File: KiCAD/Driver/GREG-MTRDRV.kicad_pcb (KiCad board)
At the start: 2 copper layers, 85 parts, among them J1 MOTOR1, J2 MOTOR2, J3 MOTOR1, J4 MOTOR2, J5 MOTOR1, J6 MOTOR2, J7 XT60-M, SW1 SW_Push, U1 STM32G474RETx, U2 DRV8262DDWR, U3 DRV8262DDWR, U4 DRV8262DDWR, U5 TPS543B20RVFT, U6 LMR51430, Y1 24MHz

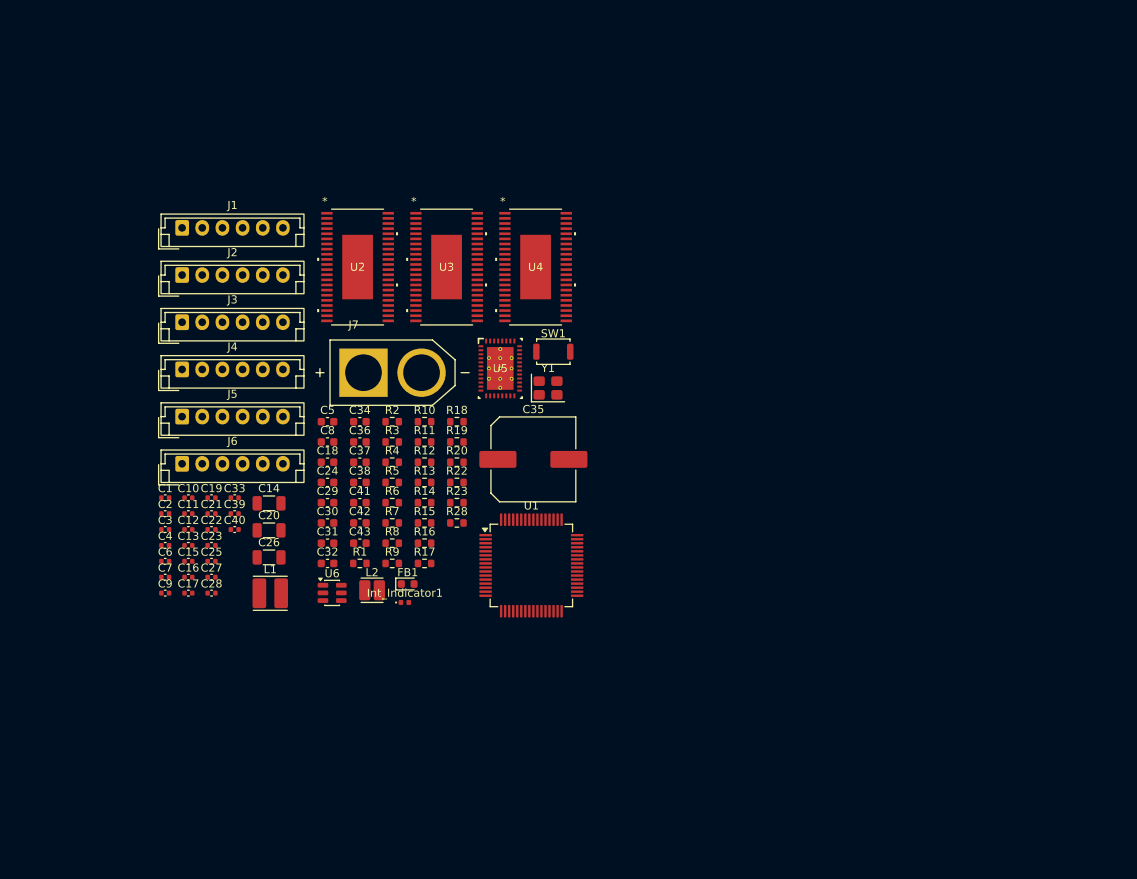
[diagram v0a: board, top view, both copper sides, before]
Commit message: Add journal and update readme
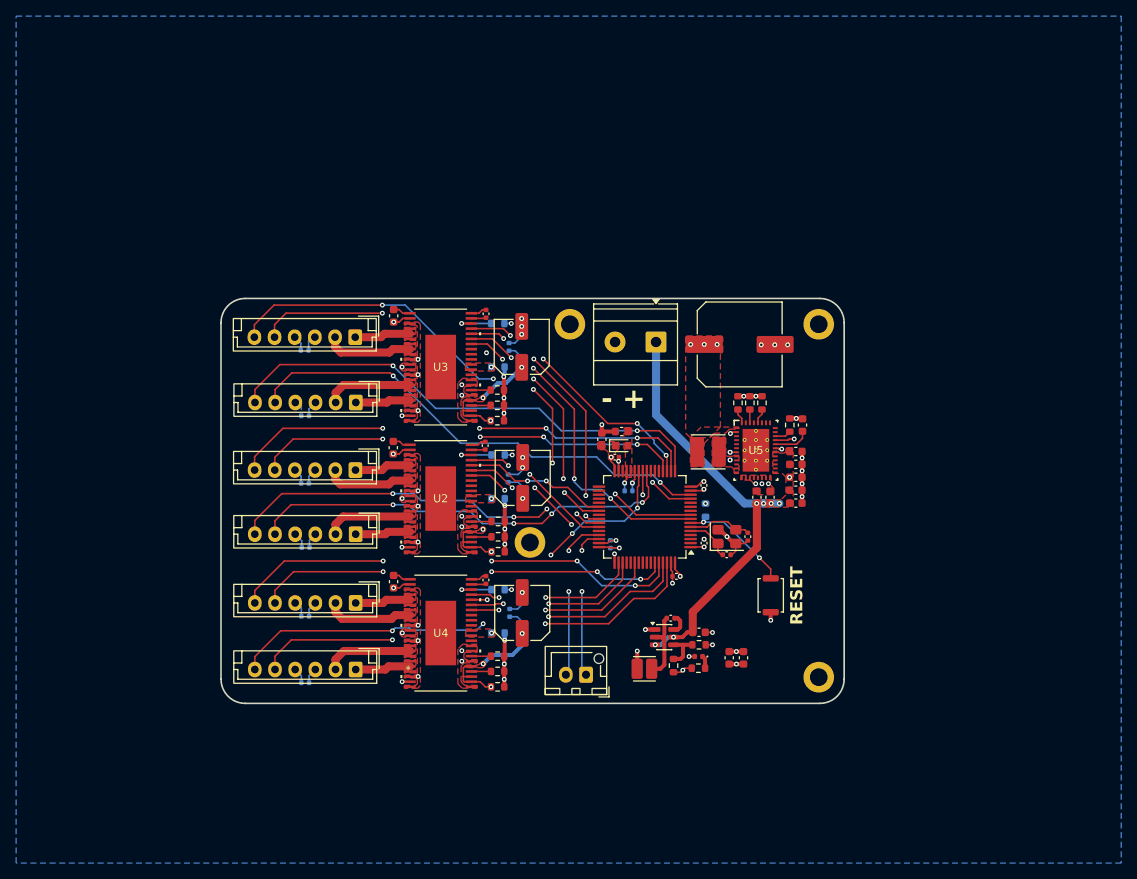
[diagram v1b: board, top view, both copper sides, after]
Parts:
- added J8: Conn_01x02_Pin, 2PinJST:JST_XH_B2B-XH-AM_1x02_P2.50mm_Vertical, F.Cu at (170.7, 131.7)
- added REF**: MountingHole_2.2mm_M2_DIN965_Pad, MountingHole:MountingHole_2.2mm_M2_DIN965_Pad, F.Cu at (163.7, 115.2)
- added REF**: MountingHole_2.2mm_M2_DIN965_Pad, MountingHole:MountingHole_2.2mm_M2_DIN965_Pad, F.Cu at (199.5, 88.2)
- added REF**: MountingHole_2.2mm_M2_DIN965_Pad, MountingHole:MountingHole_2.2mm_M2_DIN965_Pad, F.Cu at (199.5, 131.9)
- added REF**: MountingHole_2.2mm_M2_DIN965_Pad, MountingHole:MountingHole_2.2mm_M2_DIN965_Pad, F.Cu at (168.7, 88.2)
- C12: footprint Capacitor_SMD:C_0402_1005Metric -> Capacitor_SMD:C_0603_1608Metric
- C13, C15, C16, C19, C21, C22, C25, C27, C28, C3, C33, C39, C7, R1, R12, R13, R2, R4, R7, R8: moved to B.Cu
- C14, C20, C26: footprint Capacitor_SMD:C_1206_3216Metric -> Capacitor_SMD:C_Elec_6.3x7.7
- J7: value XT60-M -> PWR; footprint footprint:AMASS_XT60-M -> TerminalBlock_Phoenix:TerminalBlock_Phoenix_MKDS-1,5-2-5.08_1x02_P5.08mm_Horizontal
- moved C9 72.6 mm to (190.7, 114.5), turned to -90 degrees
- moved C10 67.1 mm to (188.1, 116.8)
- moved C2 66.9 mm to (185.3, 108.2), turned to -90 degrees
- moved C6 66.8 mm to (185.3, 115.3), turned to 90 degrees
- moved C4 63.5 mm to (181.8, 119.5), turned to 180 degrees
- moved C33 61.6 mm to (188.5, 104.5), turned to -90 degrees
- moved C32 59.7 mm to (196.7, 104.0)
- moved C31 58.4 mm to (196.7, 108.8)
- moved C7 58.4 mm to (175.9, 108.8)
- moved C29 58.1 mm to (196.7, 107.2)
- moved C30 58.1 mm to (196.7, 110.4)
- moved L1 57.0 mm to (185.8, 104.0), turned to 180 degrees
- moved C1 56.0 mm to (174.2, 104.7)
- moved C3 55.2 mm to (173.7, 115.5), turned to 90 degrees
- moved C40 55.2 mm to (181.2, 124.6), turned to 180 degrees
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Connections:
- C11 pad 1: /CPL1 -> /C1PL1
- C11 pad 2: /CPH1 -> /C1PH1
- C12 pad 2: +3.3V -> VCC
- C13 pad 1: +3.3V -> VCC
- C14 pad 1: +3.3V -> VCC
- C17 pad 1: /CPL1 -> /C2PL1
- C17 pad 2: /CPH1 -> /C2PH1
- C18 pad 1: /VCP1 -> /VCP2
- C18 pad 2: +3.3V -> VCC
- C19 pad 1: +3.3V -> VCC
- C20 pad 1: +3.3V -> VCC
- C23 pad 1: /CPL1 -> /C3PL1
- C23 pad 2: /CPH1 -> /C3PH1
- C24 pad 1: /VCP1 -> /VCP3
- C24 pad 2: +3.3V -> VCC
- C25 pad 1: +3.3V -> VCC
- C26 pad 1: +3.3V -> VCC
- C29 pad 1: +3.3V -> VCC
- C30 pad 1: +3.3V -> VCC
- C31 pad 1: +3.3V -> VCC
- C32 pad 1: +3.3V -> VCC
- C34 pad 1: GNDA -> GND
- C34 pad 2: +3.3V -> VCC
- C35 pad 2: GNDA -> GND
- C37 pad 1: +3.3V -> VCC
- C38 pad 1: +3.3V -> VCC
- C43 pad 1: +3.3V -> VCC
- R11 pad 2: /DVDD -> VCC
- R16 pad 2: /DVDD -> VCC
- R17 pad 2: GNDA -> GND
- R18 pad 1: GNDA -> GND
- R19 pad 1: GNDA -> GND
- R20 pad 1: GNDA -> GND
- R6 pad 2: /DVDD -> VCC
- U2 pad 1: /VCP1 -> /VCP2
- U2 pad 11: +3.3V -> VCC
- U2 pad 12: +3.3V -> VCC
- U2 pad 2: +3.3V -> VCC
- U2 pad 21: +3.3V -> VCC
- U2 pad 24: /DVDD -> VCC
- U2 pad 25: +3.3V -> VCC
- U2 pad 27: /DVDD -> VCC
- U2 pad 43: /CPL1 -> /C2PL1
- U2 pad 44: /CPH1 -> /C2PH1
- U3 pad 11: +3.3V -> VCC
- U3 pad 12: +3.3V -> VCC
- U3 pad 2: +3.3V -> VCC
- U3 pad 21: +3.3V -> VCC
- U3 pad 24: /DVDD -> VCC
- U3 pad 25: +3.3V -> VCC
- U3 pad 27: /DVDD -> VCC
- U3 pad 43: /CPL1 -> /C1PL1
- U3 pad 44: /CPH1 -> /C1PH1
- U4 pad 1: /VCP1 -> /VCP3
- U4 pad 11: +3.3V -> VCC
- U4 pad 12: +3.3V -> VCC
- U4 pad 2: +3.3V -> VCC
- U4 pad 21: +3.3V -> VCC
- U4 pad 24: /DVDD -> VCC
- U4 pad 25: +3.3V -> VCC
- U4 pad 27: /DVDD -> VCC
- U4 pad 43: /CPL1 -> /C3PL1
- U4 pad 44: /CPH1 -> /C3PH1
- U5 pad 21: +3.3V -> VCC
- U5 pad 22: +3.3V -> VCC
- U5 pad 23: +3.3V -> VCC
- U5 pad 24: +3.3V -> VCC
- U5 pad 25: +3.3V -> VCC
- U5 pad 26: +3.3V -> VCC
- U5 pad 29: GNDA -> GND
- U6 pad 3: +3.3V -> VCC
- U6 pad 5: +3.3V -> VCC
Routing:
- net VCC: track 0.00 -> 218.4 mm, vias 0 -> 25
- net /ENC1B: track 0.00 -> 66.5 mm, vias 0 -> 3
- net GND: track 0.00 -> 63.5 mm, vias 0 -> 50
- net /ENC2B: track 0.00 -> 62.4 mm, vias 0 -> 2
- net /ENC2A: track 0.00 -> 60.2 mm, vias 0 -> 2
- net /ENC1A: track 0.00 -> 60.2 mm, vias 0 -> 5
- net /ENC6B: track 0.00 -> 59.5 mm, vias 0 -> 3
- net /ENC3B: track 0.00 -> 58.4 mm, vias 0 -> 4
- net /ENC5B: track 0.00 -> 56.6 mm, vias 0 -> 4
- net /ENC4B: track 0.00 -> 56.5 mm, vias 0 -> 4
- net /ENC6A: track 0.00 -> 55.9 mm, vias 0 -> 2
- net /ENC4A: track 0.00 -> 54.4 mm, vias 0 -> 4
- net /ENC3A: track 0.00 -> 53.3 mm, vias 0 -> 4
- net /ENC5A: track 0.00 -> 51.5 mm, vias 0 -> 4
- net /M1_IN2: track 0.00 -> 42.0 mm, vias 0 -> 4
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- added copper zone on F.Cu, net +3.3V
- added copper zone on In1.Cu, net +3.3V
- added copper zone on B.Cu, net +5V
- added copper zone on F.Cu, net /M1OUT1
- added copper zone on F.Cu, net /M1OUT2
- added copper zone on F.Cu, net /M2OUT1
- added copper zone on F.Cu, net /M2OUT2
- added copper zone on F.Cu, net /M3OUT1
- added copper zone on F.Cu, net /M3OUT2
- added copper zone on F.Cu, net /M4OUT1
- added copper zone on F.Cu, net /M4OUT2
- added copper zone on F.Cu, net /M5OUT1
- added copper zone on F.Cu, net /M5OUT2
- added copper zone on F.Cu, net /M6OUT1
- added copper zone on F.Cu, net /M6OUT2
- added copper zone on F.Cu, net GND
- added copper zone on In2.Cu, net GND
- added copper zone on F.Cu, net Net-(C33-Pad2)
- added copper zone on F.Cu, net Net-(R13-Pad2)
- added copper zone on F.Cu, net Net-(R4-Pad2)
- added copper zone on F.Cu, net Net-(R8-Pad2)
- added copper zone on F.Cu, net PWR
- added copper zone on F.Cu, net VCC
- added copper zone on F.Cu, net VDDA
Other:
- board outline added: 77.2 x 50.2 mm
- copper layers 2 -> 4
- board text added: "- +"
- board text added: "CAN RX"
- board text added: "CAN TX"
- board text added: "MOTOR 1"
- board text added: "MOTOR 2"
- board text added: "MOTOR 3"
- board text added: "MOTOR 4"
- board text added: "MOTOR 5"
- board text added: "MOTOR 6"
- board text added: "RESET"
